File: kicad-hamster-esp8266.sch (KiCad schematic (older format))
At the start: 28 parts

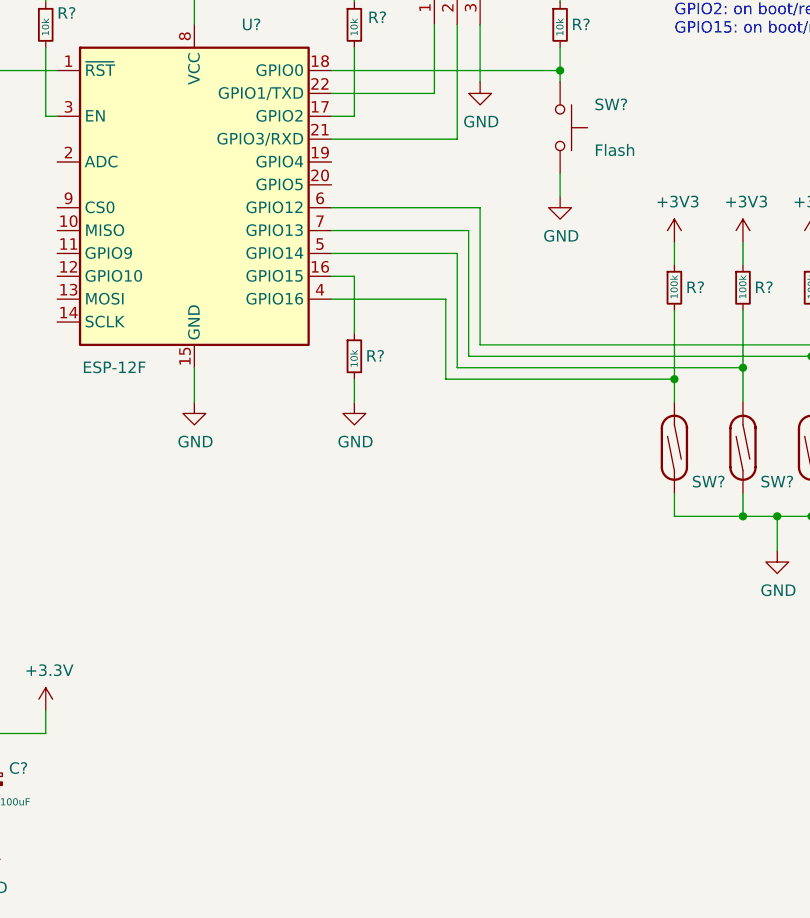
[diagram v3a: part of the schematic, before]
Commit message: Add LM75A i2c temperature sensor
Signed-off-by: Sergey Matyukevich <geomatsi@gmail.com>
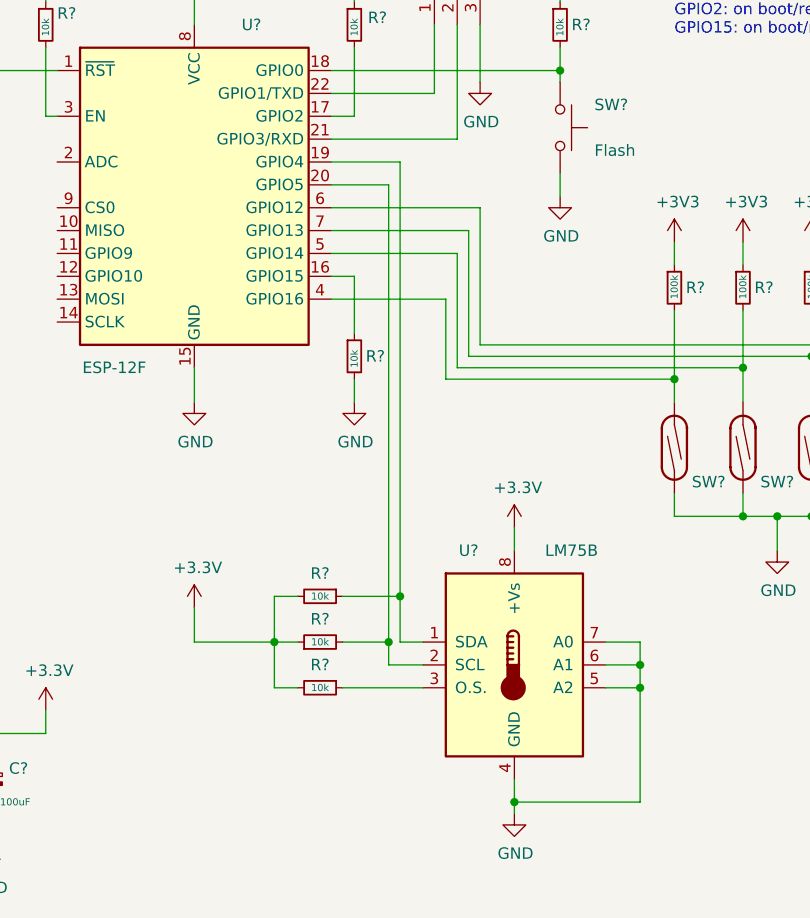
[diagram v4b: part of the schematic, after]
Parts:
- added R? (x3): 10k, symbol Device:R_Small
- added U?: LM75B, symbol Sensor_Temperature:LM75B
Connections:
- net +3V3: now also R?.1, R?.2, R?.2, U?.8 (+Vs)
- net GND: now also U?.4 (GND), U?.5 (A2), U?.6 (A1), U?.7 (A0)
- net at U?.19 (GPIO4): now also R?.1, U?.1 (SDA)
- net at U?.20 (GPIO5): now also R?.2, U?.2 (SCL)
- new net: R?.1, U?.3 (O.S.)
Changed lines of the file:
@@
 	0    -1   -1   0
 $EndComp
+$Comp
+L Sensor_Temperature:LM75B U?
+U 1 1 5F136618
+P 6900 5300
+F 0 "U?" H 6700 5800 50  0000 C CNN
+F 1 "LM75B" H 7150 5800 50  0000 C CNN
+F 2 "" H 6900 5300 50  0001 C CNN
+F 3 "http://www.ti.com/lit/ds/symlink/lm75b.pdf" H 6900 5300 50  0001 C CNN
+	1    6900 5300
+	1    0    0    -1
+$EndComp
+Wire Wire Line
+	6100 3100 6400 3100
+Wire Wire Line
+	6400 3100 6400 5000
+Wire Wire Line
+	6400 5200 6500 5200
+Wire Wire Line
+	6500 5300 6350 5300
+Wire Wire Line
+	6350 5300 6350 5200
+Wire Wire Line
+	6350 3200 6100 3200
+$Comp
+L power:GND #PWR?
+U 1 1 5F14CEE6
+P 6900 5950
+F 0 "#PWR?" H 6900 5700 50  0001 C CNN
+F 1 "GND" H 6905 5775 50  0000 C CNN
+F 2 "" H 6900 5950 50  0001 C CNN
+F 3 "" H 6900 5950 50  0001 C CNN
+	1    6900 5950
+	1    0    0    -1
+$EndComp
+Wire Wire Line
+	6900 5950 6900 5900
+Wire Wire Line
+	7300 5200 7450 5200
+Wire Wire Line
+	7450 5200 7450 5300
+Wire Wire Line
+	7450 5900 6900 5900
+Connection ~ 6900 5900
+Wire Wire Line
+	6900 5900 6900 5800
+Wire Wire Line
+	7300 5300 7450 5300
+Connection ~ 7450 5300
+Wire Wire Line
+	7450 5300 7450 5400
+Wire Wire Line
+	7300 5400 7450 5400
+Connection ~ 7450 5400
+Wire Wire Line
+	7450 5400 7450 5900
+$Comp
+L power:+3.3V #PWR?
+U 1 1 5F15B8BD
+P 6900 4700
+F 0 "#PWR?" H 6900 4550 50  0001 C CNN
+F 1 "+3.3V" H 6915 4875 50  0000 C CNN
+F 2 "" H 6900 4700 50  0001 C CNN
+F 3 "" H 6900 4700 50  0001 C CNN
+	1    6900 4700
+	1    0    0    -1
+$EndComp
+$Comp
+L Device:R_Small R?
+U 1 1 5F15C23F
+P 6050 5200
+F 0 "R?" V 6150 5200 50  0000 C CNN
+F 1 "10k" V 6050 5200 31  0000 C CNN
+F 2 "" H 6050 5200 50  0001 C CNN
+F 3 "~" H 6050 5200 50  0001 C CNN
+	1    6050 5200
+	0    -1   -1   0
+$EndComp
+$Comp
+L Device:R_Small R?
+U 1 1 5F15CBB1
+P 6050 5400
+F 0 "R?" V 5950 5400 50  0000 C CNN
+F 1 "10k" V 6050 5400 31  0000 C CNN
+F 2 "" H 6050 5400 50  0001 C CNN
+F 3 "~" H 6050 5400 50  0001 C CNN
+	1    6050 5400
+	0    1    1    0
+$EndComp
+$Comp
+L Device:R_Small R?
+U 1 1 5F15D534
+P 6050 5000
+F 0 "R?" V 5950 5000 50  0000 C CNN
+F 1 "10k" V 6050 5000 31  0000 C CNN
+F 2 "" H 6050 5000 50  0001 C CNN
+F 3 "~" H 6050 5000 50  0001 C CNN
+	1    6050 5000
+	0    1    1    0
+$EndComp
+Wire Wire Line
+	6900 4800 6900 4700
+Wire Wire Line
+	6500 5400 6150 5400
+$Comp
+L power:+3.3V #PWR?
+U 1 1 5F18662F
+P 5500 5050
+F 0 "#PWR?" H 5500 4900 50  0001 C CNN
+F 1 "+3.3V" H 5515 5225 50  0000 C CNN
+F 2 "" H 5500 5050 50  0001 C CNN
+F 3 "" H 5500 5050 50  0001 C CNN
+	1    5500 5050
+	1    0    0    -1
+$EndComp
+Wire Wire Line
+	6150 5000 6400 5000
+Connection ~ 6400 5000
+Wire Wire Line
+	6400 5000 6400 5200
+Wire Wire Line
+	6150 5200 6350 5200
+Connection ~ 6350 5200
+Wire Wire Line
+	6350 5200 6350 3200
+Wire Wire Line
+	5500 5050 5500 5200
+Wire Wire Line
+	5500 5200 5850 5200
+Wire Wire Line
+	5950 5000 5850 5000
+Wire Wire Line
+	5850 5000 5850 5200
+Connection ~ 5850 5200
+Wire Wire Line
+	5850 5200 5950 5200
+Wire Wire Line
+	5950 5400 5850 5400
+Wire Wire Line
+	5850 5400 5850 5200
 $EndSCHEMATC

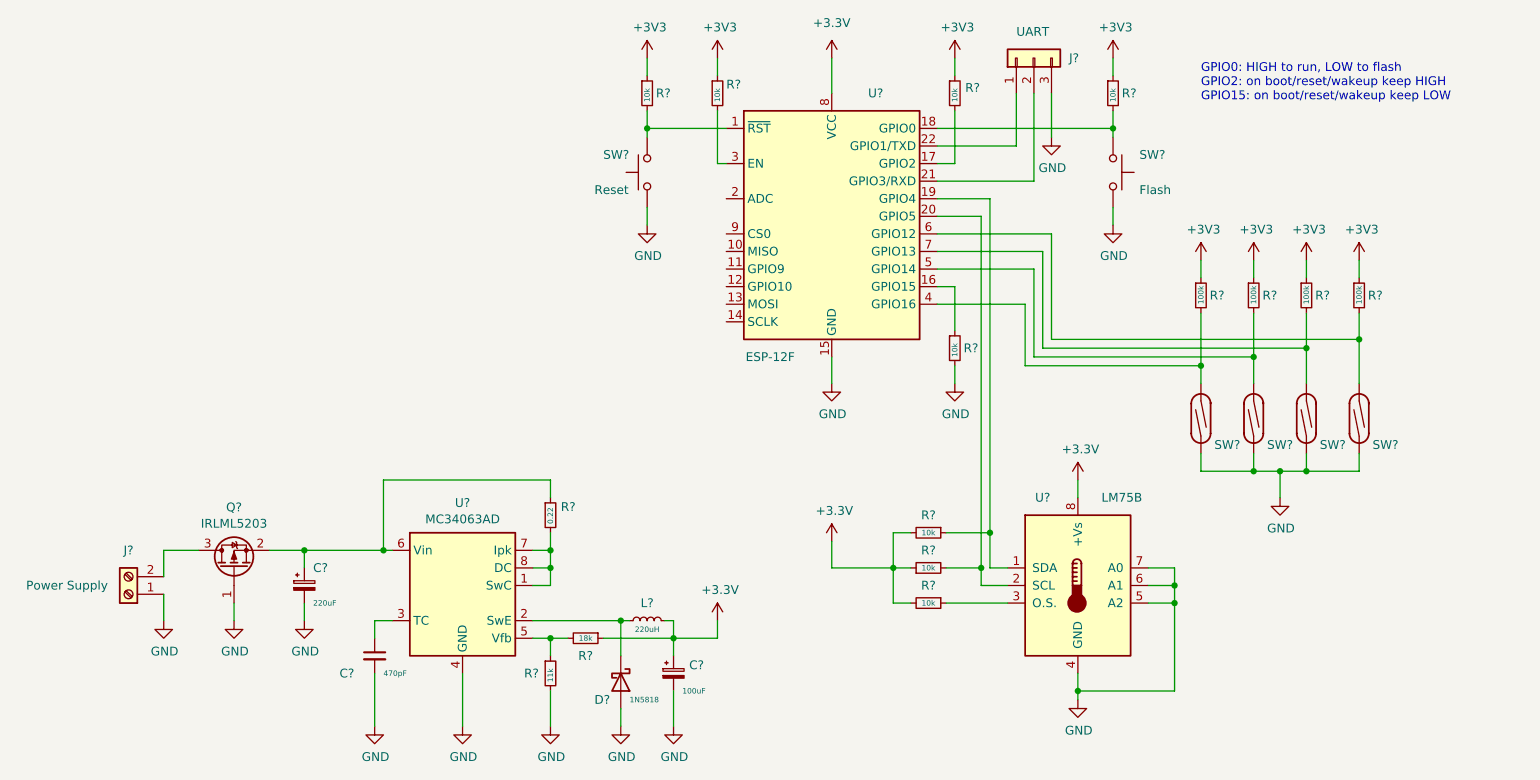
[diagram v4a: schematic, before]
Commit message: add external watchdog circuit
Signed-off-by: Sergey Matyukevich <geomatsi@gmail.com>
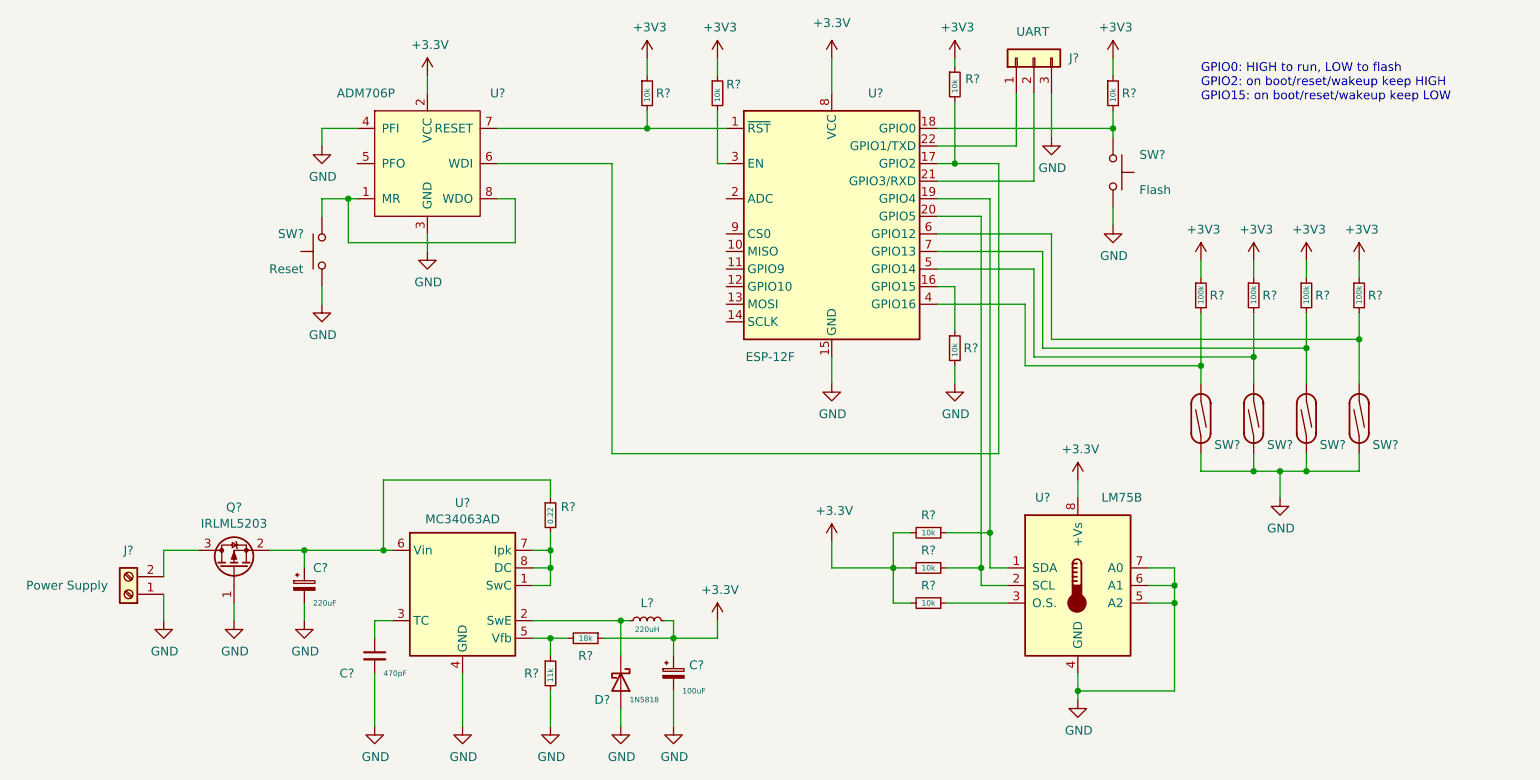
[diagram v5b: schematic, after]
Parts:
- added U?: ADM706P, Package_SO:SOIC-8_3.9x4.9mm_P1.27mm, symbol hamster-v2:ADM706P
- U?: footprint (none) -> Package_SO:SOIC-8_3.9x4.9mm_P1.27mm
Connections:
- net +3V3: now also U?.2 (VCC)
- net GND: now also U?.3 (GND), U?.4 (PFI)
- net at R?.2, U?.1 (~RST): now also U?.7 (RESET); no longer SW?.2
- net at R?.2, U?.17 (GPIO2): now also U?.6 (WDI)
- new net: SW?.2, U?.1 (MR), U?.8 (WDO)
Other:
- moved on the sheet: R?, SW?
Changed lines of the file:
@@
 L Switch:SW_Push SW?
 U 1 1 5F0DC134
-P 4450 2950
-F 0 "SW?" V 4550 3200 50  0000 R CNN
-F 1 "Reset" V 4350 3250 50  0000 R CNN
-F 2 "" H 4450 3150 50  0001 C CNN
-F 3 "~" H 4450 3150 50  0001 C CNN
-	1    4450 2950
+P 2600 3400
+F 0 "SW?" V 2700 3650 50  0000 R CNN
+F 1 "Reset" V 2500 3700 50  0000 R CNN
+F 2 "" H 2600 3600 50  0001 C CNN
+F 3 "~" H 2600 3600 50  0001 C CNN
+	1    2600 3400
 	0    -1   -1   0
 $EndComp
@@
 L power:GND #PWR?
 U 1 1 5F0E3237
-P 4450 3250
-F 0 "#PWR?" H 4450 3000 50  0001 C CNN
-F 1 "GND" H 4455 3075 50  0000 C CNN
-F 2 "" H 4450 3250 50  0001 C CNN
-F 3 "" H 4450 3250 50  0001 C CNN
-	1    4450 3250
+P 2600 3700
+F 0 "#PWR?" H 2600 3450 50  0001 C CNN
+F 1 "GND" H 2605 3525 50  0000 C CNN
+F 2 "" H 2600 3700 50  0001 C CNN
+F 3 "" H 2600 3700 50  0001 C CNN
+	1    2600 3700
 	1    0    0    -1
 $EndComp
@@
 Wire Wire Line
 	7100 3150 7100 3250
-Wire Wire Line
-	4450 3250 4450 3150
-Wire Wire Line
-	4450 2750 4450 2700
-Wire Wire Line
-	4450 2700 4900 2700
-Connection ~ 4450 2700
-Wire Wire Line
-	4450 2700 4450 2600
 Wire Wire Line
 	6100 2700 7100 2700
@@
 L Device:R_Small R?
 U 1 1 5F11DB1E
-P 6200 2500
-F 0 "R?" H 6259 2531 50  0000 L CNN
-F 1 "10k" V 6200 2450 31  0000 L CNN
-F 2 "" H 6200 2500 50  0001 C CNN
-F 3 "~" H 6200 2500 50  0001 C CNN
-	1    6200 2500
+P 6200 2450
+F 0 "R?" H 6259 2481 50  0000 L CNN
+F 1 "10k" V 6200 2400 31  0000 L CNN
+F 2 "" H 6200 2450 50  0001 C CNN
+F 3 "~" H 6200 2450 50  0001 C CNN
+	1    6200 2450
 	1    0    0    -1
 $EndComp
@@
 $EndComp
 Wire Wire Line
-	6200 2300 6200 2400
-Wire Wire Line
-	6200 2600 6200 2900
+	6200 2300 6200 2350
+Wire Wire Line
+	6200 2550 6200 2900
 Wire Wire Line
 	6200 2900 6100 2900
@@
 F 0 "U?" H 6700 5800 50  0000 C CNN
 F 1 "LM75B" H 7150 5800 50  0000 C CNN
-F 2 "" H 6900 5300 50  0001 C CNN
+F 2 "Package_SO:SOIC-8_3.9x4.9mm_P1.27mm" H 6900 5300 50  0001 C CNN
 F 3 "http://www.ti.com/lit/ds/symlink/lm75b.pdf" H 6900 5300 50  0001 C CNN
 	1    6900 5300
@@
 Wire Wire Line
 	5850 5400 5850 5200
+$Comp
+L hamster-v2:ADM706P U?
+U 1 1 5F1D7B13
+P 3200 2900
+F 0 "U?" H 3600 3300 50  0000 C CNN
+F 1 "ADM706P" H 2850 3300 50  0000 C CNN
+F 2 "Package_SO:SOIC-8_3.9x4.9mm_P1.27mm" H 3300 2350 50  0001 C CNN
+F 3 "https://static.chipdip.ru/lib/273/DOC005273190.pdf" H 3200 2900 50  0001 C CNN
+	1    3200 2900
+	1    0    0    -1
+$EndComp
+Wire Wire Line
+	3600 2700 4450 2700
+Wire Wire Line
+	4450 2600 4450 2700
+Connection ~ 4450 2700
+Wire Wire Line
+	4450 2700 4900 2700
+$Comp
+L power:+3.3V #PWR?
+U 1 1 5F1F7E63
+P 3200 2400
+F 0 "#PWR?" H 3200 2250 50  0001 C CNN
+F 1 "+3.3V" H 3215 2575 50  0000 C CNN
+F 2 "" H 3200 2400 50  0001 C CNN
+F 3 "" H 3200 2400 50  0001 C CNN
+	1    3200 2400
+	1    0    0    -1
+$EndComp
+$Comp
+L power:GND #PWR?
+U 1 1 5F1F863C
+P 3200 3400
+F 0 "#PWR?" H 3200 3150 50  0001 C CNN
+F 1 "GND" H 3205 3225 50  0000 C CNN
+F 2 "" H 3200 3400 50  0001 C CNN
+F 3 "" H 3200 3400 50  0001 C CNN
+	1    3200 3400
+	1    0    0    -1
+$EndComp
+Wire Wire Line
+	3200 3300 3200 3400
+Wire Wire Line
+	2600 3200 2600 3100
+Wire Wire Line
+	2600 3100 2750 3100
+Wire Wire Line
+	2600 3700 2600 3600
+Wire Wire Line
+	3600 3100 3700 3100
+Wire Wire Line
+	3700 3100 3700 3350
+Wire Wire Line
+	3700 3350 2750 3350
+Wire Wire Line
+	2750 3350 2750 3100
+Connection ~ 2750 3100
+Wire Wire Line
+	2750 3100 2800 3100
+$Comp
+L power:GND #PWR?
+U 1 1 5F2121E8
+P 2600 2800
+F 0 "#PWR?" H 2600 2550 50  0001 C CNN
+F 1 "GND" H 2605 2625 50  0000 C CNN
+F 2 "" H 2600 2800 50  0001 C CNN
+F 3 "" H 2600 2800 50  0001 C CNN
+	1    2600 2800
+	1    0    0    -1
+$EndComp
+Wire Wire Line
+	2600 2800 2600 2700
+Wire Wire Line
+	2600 2700 2800 2700
+Wire Wire Line
+	3200 2400 3200 2500
+Wire Wire Line
+	3600 2900 4250 2900
+Wire Wire Line
+	4250 2900 4250 4550
+Wire Wire Line
+	4250 4550 6450 4550
+Wire Wire Line
+	6450 4550 6450 2900
+Wire Wire Line
+	6450 2900 6200 2900
+Connection ~ 6200 2900
 $EndSCHEMATC
